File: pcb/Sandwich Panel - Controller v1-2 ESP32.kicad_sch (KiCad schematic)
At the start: 31 parts, among them J1 Conn_01x02_Male, J2 Conn_01x02_Male, J3 Conn_01x03_Male, J4 Conn_01x04, J5 USB_C_Receptacle_USB2.0, M1 Reflection_Pad, U1 ESP32-S3-MINI-1-N8, U2 SPX3819M5-L-3-3

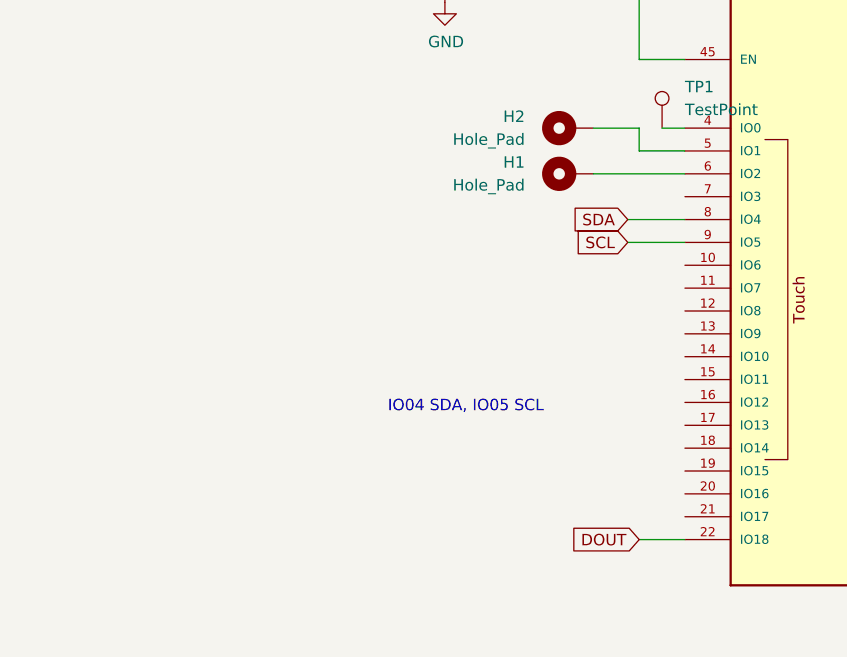
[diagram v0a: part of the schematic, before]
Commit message: Imported SMD microphone, a bunch of footprints are missing (Pancake library)
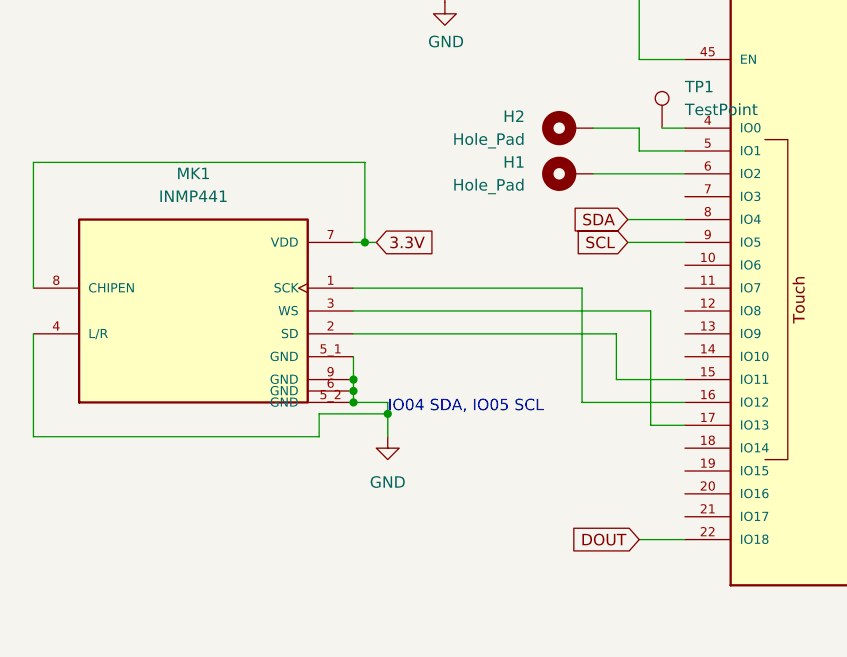
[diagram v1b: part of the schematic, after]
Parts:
- added MK1: INMP441, inmp441:MIC_INMP441, symbol INMP441:INMP441
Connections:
- net +3V3: now also MK1.7 (VDD), MK1.8 (CHIPEN)
- net GND: now also MK1.4 (L/R), MK1.5_1 (GND), MK1.5_2 (GND), MK1.6 (GND), MK1.9 (GND)
- net at U1.15 (IO11): now also MK1.2 (SD)
- net at U1.16 (IO12): now also MK1.1 (SCK)
- net at U1.17 (IO13): now also MK1.3 (WS)

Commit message: Change custom testpoints for those present in the default KiCad library
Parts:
- TP1, TP2, TP3, TP4, TP5, TP6, TP7: footprint Pancake:TestPoint_Pad_D1.0mm -> TestPoint:TestPoint_Pad_D1.0mm
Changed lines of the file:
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@@
 			)
 		)
-		(property "Footprint" "Pancake:TestPoint_Pad_D1.0mm"
+		(property "Footprint" "TestPoint:TestPoint_Pad_D1.0mm"
 			(at 130.81 143.51 0)
 			(effects
@@
 			)
 		)
-		(property "Footprint" "Pancake:TestPoint_Pad_D1.0mm"
+		(property "Footprint" "TestPoint:TestPoint_Pad_D1.0mm"
 			(at 130.81 140.97 0)
 			(effects
@@
 			)
 		)
-		(property "Footprint" "Pancake:TestPoint_Pad_D1.0mm"
+		(property "Footprint" "TestPoint:TestPoint_Pad_D1.0mm"
 			(at 130.81 146.05 0)
 			(effects
@@
 			)
 		)
-		(property "Footprint" "Pancake:TestPoint_Pad_D1.0mm"
+		(property "Footprint" "TestPoint:TestPoint_Pad_D1.0mm"
 			(at 97.79 130.81 0)
 			(effects
@@
 			)
 		)
-		(property "Footprint" "Pancake:TestPoint_Pad_D1.0mm"
+		(property "Footprint" "TestPoint:TestPoint_Pad_D1.0mm"
 			(at 130.81 176.53 0)
 			(effects
@@
 			)
 		)
-		(property "Footprint" "Pancake:TestPoint_Pad_D1.0mm"
+		(property "Footprint" "TestPoint:TestPoint_Pad_D1.0mm"
 			(at 130.81 179.07 0)
 			(effects
@@
 			)
 		)
-		(property "Footprint" "Pancake:TestPoint_Pad_D1.0mm"
+		(property "Footprint" "TestPoint:TestPoint_Pad_D1.0mm"
 			(at 130.81 148.59 0)
 			(effects
